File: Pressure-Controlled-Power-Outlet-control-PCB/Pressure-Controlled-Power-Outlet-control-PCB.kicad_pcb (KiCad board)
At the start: 4 copper layers, 100.3 x 82.5 mm, 25 parts, among them J1 Analog water pressure sensor 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, J2 1017514, K1 T9GV5L24-24, K2 T9GV5L24-24, Q1 2N3906, Q2 IRF540N, Q3 IRF540N, Q4 2N3906, U1 Pico, U2 LM324, U3 LF50_TO220

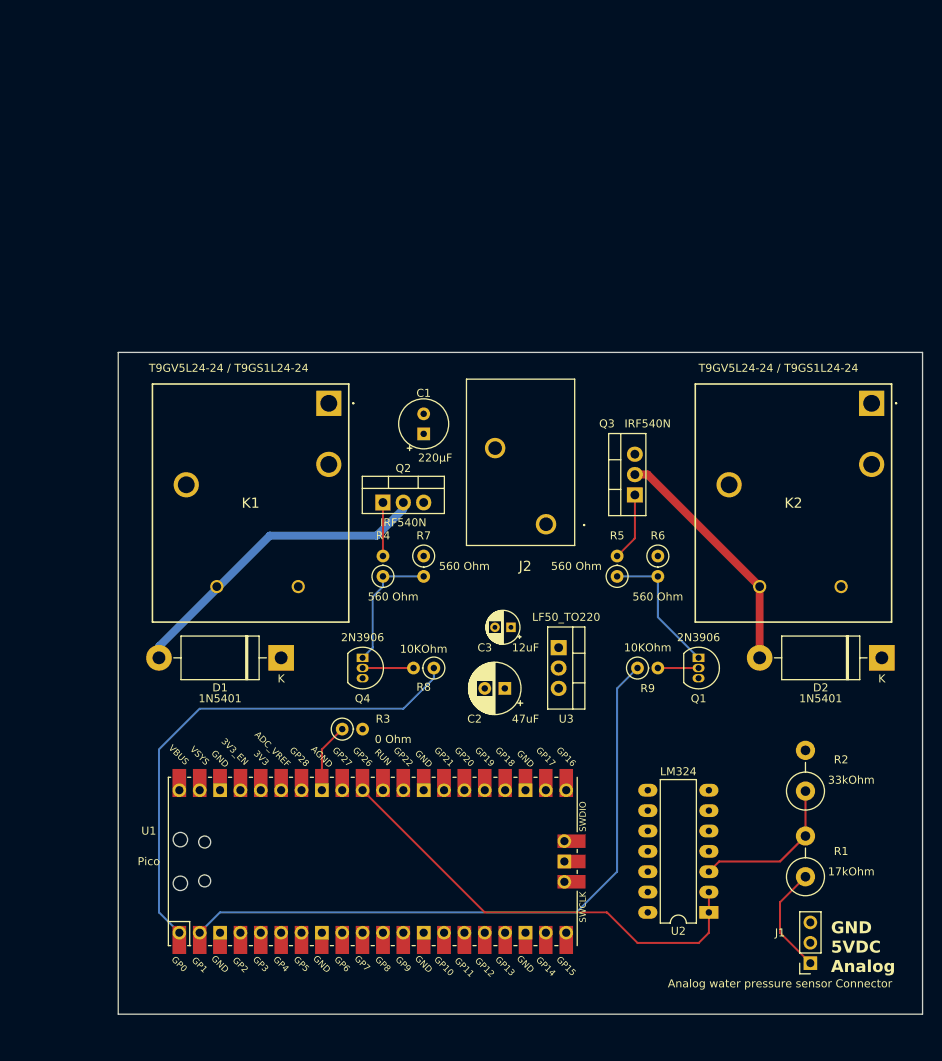
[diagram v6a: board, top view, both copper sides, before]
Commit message: fixed PCB design to allow for better spacing of parts
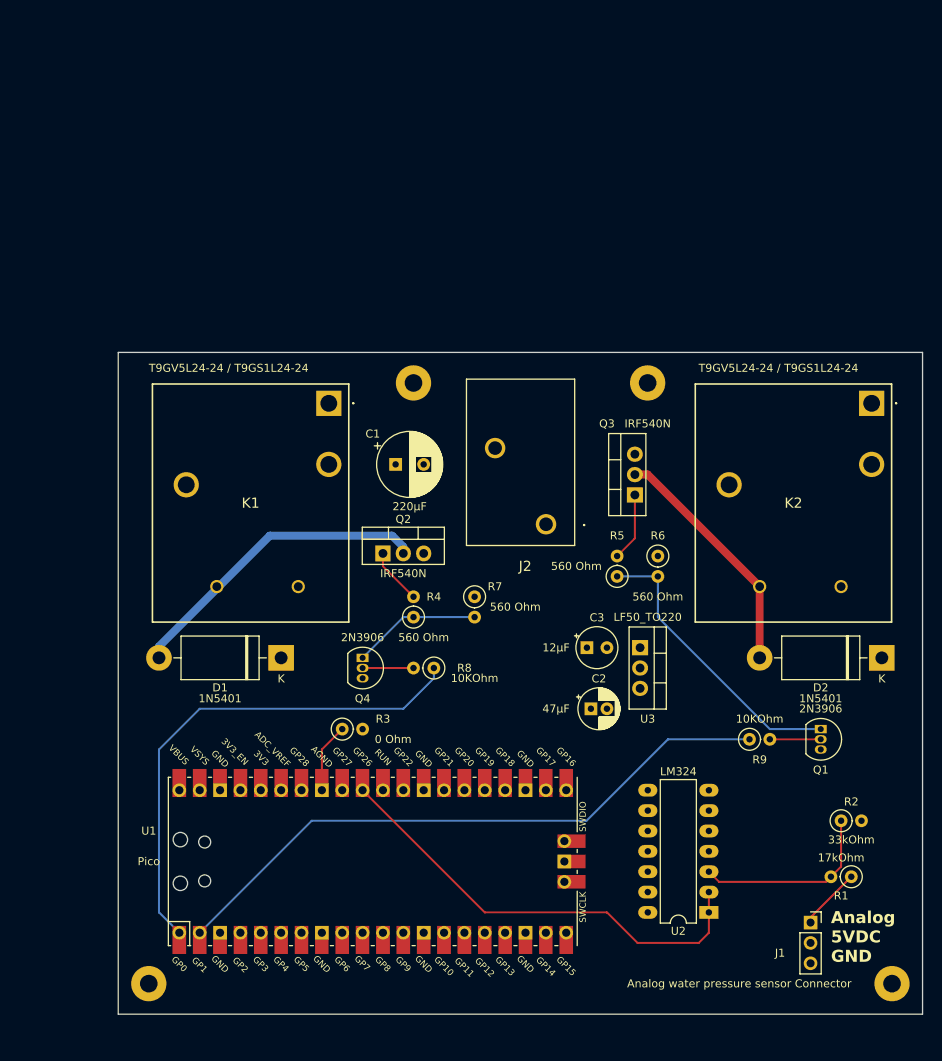
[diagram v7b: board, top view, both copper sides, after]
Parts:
- added H1: MountingHole_Pad, MountingHole:MountingHole_2.2mm_M2_Pad, F.Cu at (182.9, 144.8)
- added H2: MountingHole_Pad, MountingHole:MountingHole_2.2mm_M2_Pad, F.Cu at (90.2, 144.8)
- added H3: MountingHole_Pad, MountingHole:MountingHole_2.2mm_M2_Pad, F.Cu at (152.4, 69.8)
- added H4: MountingHole_Pad, MountingHole:MountingHole_2.2mm_M2_Pad, F.Cu at (123.2, 69.8)
- C1: footprint Capacitor_THT:CP_Radial_Tantal_D6.0mm_P2.50mm -> Capacitor_THT:CP_Radial_D8.0mm_P3.50mm
- C2: value 47uF -> 47µF; footprint Capacitor_THT:CP_Radial_D6.3mm_P2.50mm -> Capacitor_THT:CP_Radial_D5.0mm_P2.00mm
- C3: value 12uF -> 12µF; footprint Capacitor_THT:CP_Radial_D4.0mm_P2.00mm -> Capacitor_THT:CP_Radial_Tantal_D5.0mm_P2.50mm
- R1, R2: footprint Resistor_THT:R_Axial_DIN0414_L11.9mm_D4.5mm_P5.08mm_Vertical -> Resistor_THT:R_Axial_DIN0207_L6.3mm_D2.5mm_P2.54mm_Vertical
- moved Q1 17.6 mm to (174.0, 113.0)
- moved R9 16.6 mm to (165.1, 114.3)
- moved C2 11.0 mm to (145.3, 110.5), turned to 0 degrees
- moved U3 10.2 mm to (151.5, 102.9)
- moved C3 9.80 mm to (144.8, 102.9), turned to 0 degrees
- moved R7 8.13 mm to (130.8, 96.5)
- moved R4 6.35 mm to (123.2, 99.1)
- moved Q2 6.35 mm to (119.4, 91.1)
- moved R2 5.78 mm to (176.5, 124.5), turned to 0 degrees
- moved R1 5.72 mm to (177.8, 131.4), turned to 180 degrees
- moved C1 5.17 mm to (121.0, 80.0), turned to 0 degrees
- moved J1 5.07 mm to (172.7, 137.2), turned to 0 degrees
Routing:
- net Net-(Q1-E): track 17.3 -> 36.3 mm
- net /Water Pressure 5V: track 13.7 -> 7.82 mm
- net Net-(U2A-+): track 19.5 -> 23.5 mm
- net /Activate_Neutral: track 81.7 -> 78.6 mm
- net Net-(Q1-B): track 5.08 -> 6.35 mm
- net Net-(D1-A): track 39.8 -> 39.0 mm
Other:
- board text added: "Analog 5VDC GND"
- board text removed: "GND 5VDC Analog"

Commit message: forgor to save
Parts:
- added J3: I2C0 Connector, Connector_PinHeader_2.54mm:PinHeader_1x05_P2.54mm_Vertical, F.Cu at (128.3, 147.3)
- added J4: SPI1 Connector, Connector_PinHeader_2.54mm:PinHeader_1x06_P2.54mm_Vertical, F.Cu at (102.9, 147.3)
- moved H2 2.84 mm to (91.4, 147.3)
- moved H1 2.84 mm to (181.6, 147.3)
- moved H3 1.27 mm to (152.4, 71.1)
- moved H4 1.27 mm to (123.2, 71.1)
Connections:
- U1 pad 11: unconnected-(U1-GPIO8-Pad11) -> /SPI1_RX
- U1 pad 12: unconnected-(U1-GPIO9-Pad12) -> /SPI1_CSn
- U1 pad 14: unconnected-(U1-GPIO10-Pad14) -> /SPI1_TX
- U1 pad 36: unconnected-(U1-3V3-Pad36) -> +3.3V
- U1 pad 6: unconnected-(U1-GPIO4-Pad6) -> /I2C0_SDA
- U1 pad 7: unconnected-(U1-GPIO5-Pad7) -> /I2C0_SCL
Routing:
- net +3.3V: track 0.00 -> 75.2 mm
- net /I2C0_SCL: track 0.00 -> 30.4 mm
- net /I2C0_SDA: track 0.00 -> 30.4 mm
- net /SPI1_TX: track 0.00 -> 23.2 mm
- net /SPI1_RX: track 0.00 -> 16.1 mm
- net /SPI1_CSn: track 0.00 -> 13.5 mm
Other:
- board size 100.3 x 82.5 mm -> 100.3 x 86.4 mm
- board text added: "5V 3.3V RX TX CSn GND"
- board text added: "5V 3.3V SDA SCL GND"
